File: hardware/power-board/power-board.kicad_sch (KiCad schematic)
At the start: 25 parts, among them J1 SW_SPST, J2 Main Board, J3 DMX512 Out Jack, J4 DMX512, K1 SPST-NO, K2 SPST-NO, P1 IEC320-C14, P2 IEC320-C13, P3 IEC320-C13, U1 NUD3112DMT1G, U2 MAX3075E

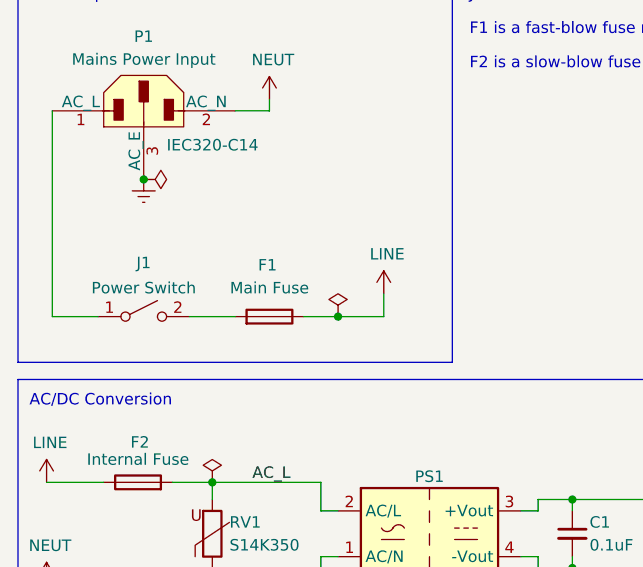
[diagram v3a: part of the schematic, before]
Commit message: Moved input fuse and changed power switch connector
The fuse is now before the power switch, which also makes routing a bit
easier.  Also switched the connector used for the power switch wires, to
something a bit less bulky.
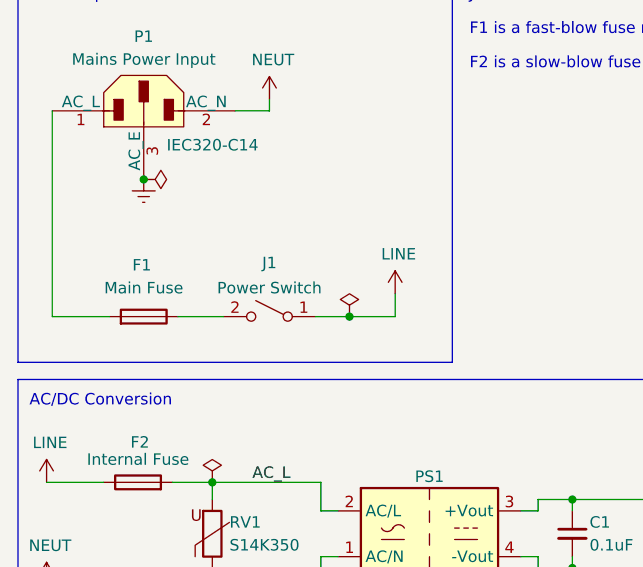
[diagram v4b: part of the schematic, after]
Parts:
- J1: footprint lib_fp:TE_MATE-N-LOK_350428-x_1x02_P6.35mm_Vertical -> Connector_Molex:Molex_Mega-Fit_76829-0002_2x01_P5.70mm_Vertical; Manufacturer TE Connectivity -> Molex; Manufacturer PN 350428-1 -> 0768290002; Supplier PN A1466-ND -> WM11975-ND
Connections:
- net LINE: now also J1.1 (A); no longer F1.1
- net at P1.1 (AC_L): now also F1.2; no longer J1.1 (A)
- net at J1.2 (B): now also F1.1; no longer F1.2
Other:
- moved on the sheet: F1, J1
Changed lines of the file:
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@@
   (junction (at 118.11 154.305) (diameter 0) (color 0 0 0 0)
   )
-  (junction (at 49.53 52.07) (diameter 0) (color 0 0 0 0)
+  (junction (at 50.8 52.07) (diameter 0) (color 0 0 0 0)
   )
   (junction (at 27.94 36.83) (diameter 0) (color 0 0 0 0)
@@
     (stroke (width 0) (type default))
   )
-  (wire (pts (xy 45.72 52.07) (xy 49.53 52.07))
+  (wire (pts (xy 46.99 52.07) (xy 50.8 52.07))
     (stroke (width 0) (type default))
   )
@@
     (stroke (width 0) (type default))
   )
-  (wire (pts (xy 33.02 52.07) (xy 38.1 52.07))
+  (wire (pts (xy 31.75 52.07) (xy 36.83 52.07))
     (stroke (width 0) (type default))
   )
@@
     (stroke (width 0) (type default))
   )
-  (wire (pts (xy 49.53 52.07) (xy 54.61 52.07))
+  (wire (pts (xy 50.8 52.07) (xy 55.88 52.07))
     (stroke (width 0) (type default))
   )
@@
     (stroke (width 0) (type default))
   )
-  (wire (pts (xy 54.61 52.07) (xy 54.61 49.53))
+  (wire (pts (xy 55.88 52.07) (xy 55.88 49.53))
     (stroke (width 0) (type default))
   )
@@
     (stroke (width 0) (type default))
   )
-  (wire (pts (xy 17.78 52.07) (xy 22.86 52.07))
+  (wire (pts (xy 17.78 52.07) (xy 24.13 52.07))
     (stroke (width 0) (type default))
   )
@@
     )
   )
-  (symbol (lib_id "Switch:SW_SPST") (at 27.94 52.07 0) (unit 1)
-    (in_bom yes) (on_board yes) (dnp no)
-    (property "Reference" "J1" (at 27.94 46.101 0)
-      (effects (font (size 1.27 1.27)))
-    )
-    (property "Value" "SW_SPST" (at 27.94 48.4124 0)
-      (effects (font (size 1.27 1.27)) hide)
-    )
-    (property "Footprint" "lib_fp:TE_MATE-N-LOK_350428-x_1x02_P6.35mm_Vertical" (at 27.94 52.07 0)
-      (effects (font (size 1.27 1.27)) hide)
-    )
-    (property "Datasheet" "https://www.te.com/commerce/DocumentDelivery/DDEController?Action=srchrtrv&DocNm=350428&DocType=Customer+Drawing&DocLang=English" (at 27.94 52.07 0)
-      (effects (font (size 1.27 1.27)) hide)
-    )
-    (property "User Label" "Power Switch" (at 27.94 48.895 0)
-      (effects (font (size 1.27 1.27)))
-    )
-    (property "Description" "CONN HEADER VERT 2POS 6.35MM" (at 27.94 52.07 0)
-      (effects (font (size 1.27 1.27)) hide)
-    )
-    (property "Manufacturer" "TE Connectivity" (at 27.94 52.07 0)
-      (effects (font (size 1.27 1.27)) hide)
-    )
-    (property "Manufacturer PN" "350428-1" (at 27.94 52.07 0)
-      (effects (font (size 1.27 1.27)) hide)
-    )
-    (property "Supplier" "Digi-Key" (at 27.94 52.07 0)
-      (effects (font (size 1.27 1.27)) hide)
-    )
-    (property "Supplier PN" "A1466-ND" (at 27.94 52.07 0)
+  (symbol (lib_id "Switch:SW_SPST") (at 41.91 52.07 0) (mirror y) (unit 1)
+    (in_bom yes) (on_board yes) (dnp no)
+    (property "Reference" "J1" (at 41.91 46.101 0)
+      (effects (font (size 1.27 1.27)))
+    )
+    (property "Value" "SW_SPST" (at 41.91 48.4124 0)
+      (effects (font (size 1.27 1.27)) hide)
+    )
+    (property "Footprint" "Connector_Molex:Molex_Mega-Fit_76829-0002_2x01_P5.70mm_Vertical" (at 41.91 52.07 0)
+      (effects (font (size 1.27 1.27)) hide)
+    )
+    (property "Datasheet" "https://www.molex.com/pdm_docs/as/AS-76823-100.pdf" (at 41.91 52.07 0)
+      (effects (font (size 1.27 1.27)) hide)
+    )
+    (property "User Label" "Power Switch" (at 41.91 48.895 0)
+      (effects (font (size 1.27 1.27)))
+    )
+    (property "Description" "CONN HEADER VERT 2POS 5.70MM" (at 41.91 52.07 0)
+      (effects (font (size 1.27 1.27)) hide)
+    )
+    (property "Manufacturer" "Molex" (at 41.91 52.07 0)
+      (effects (font (size 1.27 1.27)) hide)
+    )
+    (property "Manufacturer PN" "0768290002" (at 41.91 52.07 0)
+      (effects (font (size 1.27 1.27)) hide)
+    )
+    (property "Supplier" "Digi-Key" (at 41.91 52.07 0)
+      (effects (font (size 1.27 1.27)) hide)
+    )
+    (property "Supplier PN" "WM11975-ND" (at 41.91 52.07 0)
       (effects (font (size 1.27 1.27)) hide)
     )
@@
     )
   )
-  (symbol (lib_id "power:LINE") (at 54.61 49.53 0) (unit 1)
-    (in_bom yes) (on_board yes) (dnp no)
-    (property "Reference" "#PWR04" (at 54.61 53.34 0)
-      (effects (font (size 1.27 1.27)) hide)
-    )
-    (property "Value" "LINE" (at 54.991 45.1358 0)
-      (effects (font (size 1.27 1.27)))
-    )
-    (property "Footprint" "" (at 54.61 49.53 0)
-      (effects (font (size 1.27 1.27)) hide)
-    )
-    (property "Datasheet" "" (at 54.61 49.53 0)
+  (symbol (lib_id "power:LINE") (at 55.88 49.53 0) (unit 1)
+    (in_bom yes) (on_board yes) (dnp no)
+    (property "Reference" "#PWR04" (at 55.88 53.34 0)
+      (effects (font (size 1.27 1.27)) hide)
+    )
+    (property "Value" "LINE" (at 56.261 45.1358 0)
+      (effects (font (size 1.27 1.27)))
+    )
+    (property "Footprint" "" (at 55.88 49.53 0)
+      (effects (font (size 1.27 1.27)) hide)
+    )
+    (property "Datasheet" "" (at 55.88 49.53 0)
       (effects (font (size 1.27 1.27)) hide)
     )
@@
     )
   )
-  (symbol (lib_id "power:PWR_FLAG") (at 49.53 52.07 0) (unit 1)
-    (in_bom yes) (on_board yes) (dnp no)
-    (property "Reference" "#FLG01" (at 49.53 50.165 0)
-      (effects (font (size 1.27 1.27)) hide)
-    )
-    (property "Value" "PWR_FLAG" (at 49.53 48.26 0)
-      (effects (font (size 1.27 1.27)) hide)
-    )
-    (property "Footprint" "" (at 49.53 52.07 0)
-      (effects (font (size 1.27 1.27)) hide)
-    )
-    (property "Datasheet" "~" (at 49.53 52.07 0)
+  (symbol (lib_id "power:PWR_FLAG") (at 50.8 52.07 0) (unit 1)
+    (in_bom yes) (on_board yes) (dnp no)
+    (property "Reference" "#FLG01" (at 50.8 50.165 0)
+      (effects (font (size 1.27 1.27)) hide)
+    )
+    (property "Value" "PWR_FLAG" (at 50.8 48.26 0)
+      (effects (font (size 1.27 1.27)) hide)
+    )
+    (property "Footprint" "" (at 50.8 52.07 0)
+      (effects (font (size 1.27 1.27)) hide)
+    )
+    (property "Datasheet" "~" (at 50.8 52.07 0)
       (effects (font (size 1.27 1.27)) hide)
     )
@@
     )
   )
-  (symbol (lib_id "Device:Fuse") (at 41.91 52.07 270) (mirror x) (unit 1)
-    (in_bom yes) (on_board yes) (dnp no)
-    (property "Reference" "F1" (at 40.64 46.355 90)
-      (effects (font (size 1.27 1.27)) (justify left))
-    )
-    (property "Value" "Fuse" (at 36.83 49.53 90)
+  (symbol (lib_id "Device:Fuse") (at 27.94 52.07 270) (mirror x) (unit 1)
+    (in_bom yes) (on_board yes) (dnp no)
+    (property "Reference" "F1" (at 26.67 46.355 90)
+      (effects (font (size 1.27 1.27)) (justify left))
+    )
+    (property "Value" "Fuse" (at 22.86 49.53 90)
       (effects (font (size 1.27 1.27)) (justify left) hide)
     )
-    (property "Footprint" "Fuse:Fuseholder_Cylinder-5x20mm_Bulgin_FX0457_Horizontal_Closed" (at 41.91 53.848 90)
-      (effects (font (size 1.27 1.27)) hide)
-    )
-    (property "Datasheet" "https://www.bulgin.com/products/pub/media/bulgin/data/Fuseholders.pdf" (at 41.91 52.07 0)
-      (effects (font (size 1.27 1.27)) hide)
-    )
-    (property "User Label" "Main Fuse" (at 41.91 48.895 90)
-      (effects (font (size 1.27 1.27)))
-    )
-    (property "Description" "FUSE HLDR CARTRIDGE 250V 10A PCB" (at 41.91 52.07 0)
-      (effects (font (size 1.27 1.27)) hide)
-    )
-    (property "Manufacturer" "Bulgin" (at 41.91 52.07 0)
-      (effects (font (size 1.27 1.27)) hide)
-    )
-    (property "Manufacturer PN" "FX0457" (at 41.91 52.07 0)
-      (effects (font (size 1.27 1.27)) hide)
-    )
-    (property "Supplier" "Digi-Key" (at 41.91 52.07 0)
-      (effects (font (size 1.27 1.27)) hide)
-    )
-    (property "Supplier PN" "708-1898-ND" (at 41.91 52.07 0)
+    (property "Footprint" "Fuse:Fuseholder_Cylinder-5x20mm_Bulgin_FX0457_Horizontal_Closed" (at 27.94 53.848 90)
+      (effects (font (size 1.27 1.27)) hide)
+    )
+    (property "Datasheet" "https://www.bulgin.com/products/pub/media/bulgin/data/Fuseholders.pdf" (at 27.94 52.07 0)
+      (effects (font (size 1.27 1.27)) hide)
+    )
+    (property "User Label" "Main Fuse" (at 27.94 48.895 90)
+      (effects (font (size 1.27 1.27)))
+    )
+    (property "Description" "FUSE HLDR CARTRIDGE 250V 10A PCB" (at 27.94 52.07 0)
+      (effects (font (size 1.27 1.27)) hide)
+    )
+    (property "Manufacturer" "Bulgin" (at 27.94 52.07 0)
+      (effects (font (size 1.27 1.27)) hide)
+    )
+    (property "Manufacturer PN" "FX0457" (at 27.94 52.07 0)
+      (effects (font (size 1.27 1.27)) hide)
+    )
+    (property "Supplier" "Digi-Key" (at 27.94 52.07 0)
+      (effects (font (size 1.27 1.27)) hide)
+    )
+    (property "Supplier PN" "708-1898-ND" (at 27.94 52.07 0)
       (effects (font (size 1.27 1.27)) hide)
     )
@@
       (effects (font (size 1.27 1.27)) hide)
     )
+    (property "Sim.Name" "kicad_builtin_varistor" (at 35.56 76.2 0)
+      (effects (font (size 1.27 1.27)) hide)
+    )
+    (property "Sim.Device" "SUBCKT" (at 35.56 76.2 0)
+      (effects (font (size 1.27 1.27)) hide)
+    )
+    (property "Sim.Pins" "1=A 2=B" (at 35.56 76.2 0)
+      (effects (font (size 1.27 1.27)) hide)
+    )
+    (property "Sim.Params" "threshold=1k" (at 35.56 76.2 0)
+      (effects (font (size 1.27 1.27)) hide)
+    )
+    (property "Sim.Library" "${KICAD7_SYMBOL_DIR}/Simulation_SPICE.sp" (at 35.56 76.2 0)
+      (effects (font (size 1.27 1.27)) hide)
+    )

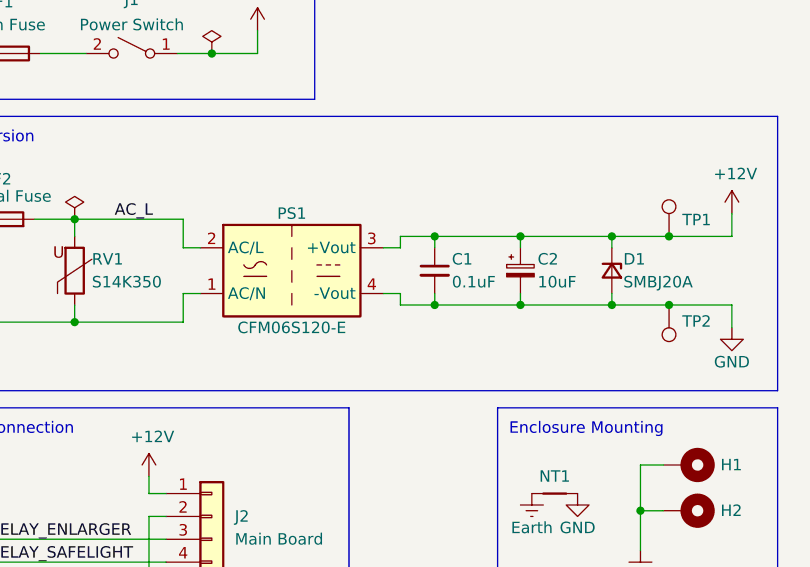
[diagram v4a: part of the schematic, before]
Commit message: Swap AC/DC converter for IRM-10-12 and update output capacitor
A bit more comfortable with this option versus the other one, since it
likely has more protection and filtering.  Still may want to rearrange
and reroute some of the output components, which are a bit cramped at
the moment.
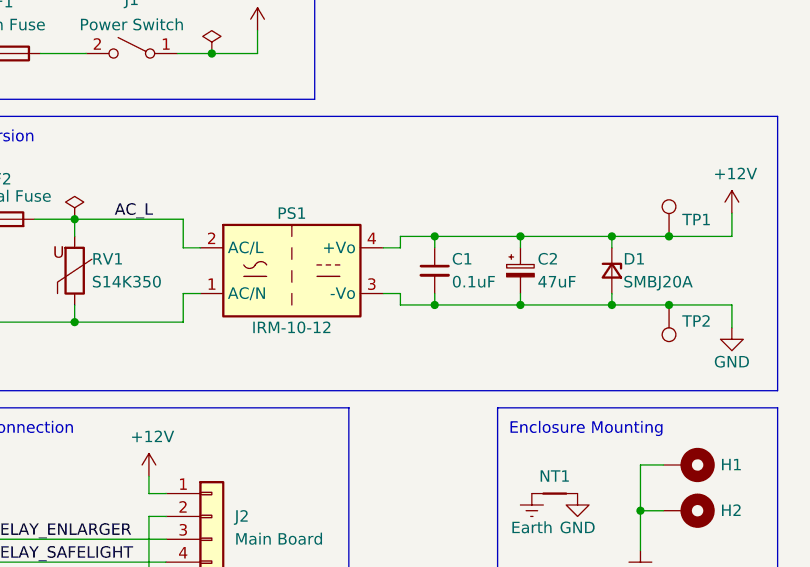
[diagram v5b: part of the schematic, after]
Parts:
- removed PS1: CFM06S120-E, lib_fp:Converter_ACDC_Cincom_CFM06Sxxx-E, symbol Project:CFM06S120-E
- added PS1: IRM-10-12, Converter_ACDC:Converter_ACDC_MeanWell_IRM-10-xx_THT, symbol Converter_ACDC:IRM-10-12
- C2: value 10uF -> 47uF; footprint Capacitor_SMD:CP_Elec_6.3x5.4 -> lib_fp:CP_Elec_8x10.2; Manufacturer PN EDK106M063A9GAA -> EDH476M063A9MAA; Supplier PN 399-6049-1-ND -> 399-18138-1-ND
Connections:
- net +12V: now also PS1.4 (+Vo)
- net AC_L: now also PS1.2 (AC/L)
- net GND: now also PS1.3 (-Vo)
- net NEUT: now also PS1.1 (AC/N)
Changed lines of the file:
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@@
-    )
-  )
-  (symbol (lib_id "Project:CFM06S120-E") (at 59.69 76.2 0) (unit 1)
-    (in_bom yes) (on_board yes) (dnp no)
-    (property "Reference" "PS1" (at 59.69 69.85 0)
-      (effects (font (size 1.27 1.27)))
-    )
-    (property "Value" "CFM06S120-E" (at 59.69 82.55 0)
-      (effects (font (size 1.27 1.27)))
-    )
-    (property "Footprint" "lib_fp:Converter_ACDC_Cincom_CFM06Sxxx-E" (at 59.69 85.09 0)
-      (effects (font (size 1.27 1.27)) hide)
-    )
-    (property "Datasheet" "https://www.cincon.com/productdownload/Datasheet-CFM06S-series.pdf" (at 59.69 86.995 0)
-      (effects (font (size 1.27 1.27)) hide)
-    )
-    (property "Description" "AC/DC CONVERTER 12V 6W" (at 59.69 76.2 0)
-      (effects (font (size 1.27 1.27)) hide)
-    )
-    (property "Manufacturer" "Cincon Electronics Co. LTD" (at 59.69 76.2 0)
-      (effects (font (size 1.27 1.27)) hide)
-    )
-    (property "Manufacturer PN" "CFM06S120-E" (at 59.69 76.2 0)
-      (effects (font (size 1.27 1.27)) hide)
-    )
-    (property "Supplier" "Digi-Key" (at 59.69 76.2 0)
-      (effects (font (size 1.27 1.27)) hide)
-    )
-    (property "Supplier PN" "2034-CFM06S120-E-ND" (at 59.69 76.2 0)
-      (effects (font (size 1.27 1.27)) hide)
-    )
-    (pin "1")
-    (pin "2")
-    (pin "3")
-    (pin "4")
-    (instances
-      (project "power-board"
-        (path "/31a301d9-d769-4a35-943a-fe3e3609e773"
-          (reference "PS1") (unit 1)
-        )
-      )
     )
   )
@@
       (effects (font (size 1.27 1.27)) (justify left))
     )
-    (property "Value" "10uF" (at 86.995 77.47 0)
-      (effects (font (size 1.27 1.27)) (justify left))
-    )
-    (property "Footprint" "Capacitor_SMD:CP_Elec_6.3x5.4" (at 85.09 76.2 0)
-      (effects (font (size 1.27 1.27)) hide)
-    )
-    (property "Datasheet" "https://content.kemet.com/datasheets/KEM_A4001_EDK.pdf" (at 85.09 76.2 0)
-      (effects (font (size 1.27 1.27)) hide)
-    )
-    (property "Description" "CAP ALUM 10UF 20% 63V SMD" (at 85.09 76.2 0)
+    (property "Value" "47uF" (at 86.995 77.47 0)
+      (effects (font (size 1.27 1.27)) (justify left))
+    )
+    (property "Footprint" "lib_fp:CP_Elec_8x10.2" (at 85.09 76.2 0)
+      (effects (font (size 1.27 1.27)) hide)
+    )
+    (property "Datasheet" "https://connect.kemet.com:7667/gateway/IntelliData-ComponentDocumentation/1.0/download/datasheet/EDH476M063A9MAA" (at 85.09 76.2 0)
+      (effects (font (size 1.27 1.27)) hide)
+    )
+    (property "Description" "CAP ALUM 47UF 20% 63V SMD" (at 85.09 76.2 0)
       (effects (font (size 1.27 1.27)) hide)
     )
@@
       (effects (font (size 1.27 1.27)) hide)
     )
-    (property "Manufacturer PN" "EDK106M063A9GAA" (at 85.09 76.2 0)
+    (property "Manufacturer PN" "EDH476M063A9MAA" (at 85.09 76.2 0)
       (effects (font (size 1.27 1.27)) hide)
     )
@@
       (effects (font (size 1.27 1.27)) hide)
     )
-    (property "Supplier PN" "399-6049-1-ND" (at 85.09 76.2 0)
+    (property "Supplier PN" "399-18138-1-ND" (at 85.09 76.2 0)
       (effects (font (size 1.27 1.27)) hide)
     )
@@
         )
       )
+    )
+  )
+  (symbol (lib_id "Converter_ACDC:IRM-10-12") (at 59.69 76.2 0) (unit 1)
+    (in_bom yes) (on_board yes) (dnp no)
+    (property "Reference" "PS1" (at 59.69 69.85 0)
+      (effects (font (size 1.27 1.27)))
+    )
+    (property "Value" "IRM-10-12" (at 59.69 82.55 0)
+      (effects (font (size 1.27 1.27)))
+    )
+    (property "Footprint" "Converter_ACDC:Converter_ACDC_MeanWell_IRM-10-xx_THT" (at 59.69 85.09 0)
+      (effects (font (size 1.27 1.27)) hide)
+    )
+    (property "Datasheet" "https://www.meanwell.com/Upload/PDF/IRM-10/IRM-10-SPEC.PDF" (at 59.69 86.36 0)
+      (effects (font (size 1.27 1.27)) hide)
+    )
+    (property "Description" "AC/DC CONVERTER 12V 10W" (at 59.69 76.2 0)
+      (effects (font (size 1.27 1.27)) hide)
+    )
+    (property "Manufacturer" "MEAN WELL" (at 59.69 76.2 0)
+      (effects (font (size 1.27 1.27)) hide)
+    )
+    (property "Manufacturer PN" "IRM-10-12" (at 59.69 76.2 0)
+      (effects (font (size 1.27 1.27)) hide)
+    )
+    (property "Supplier" "Mouser" (at 59.69 76.2 0)
+      (effects (font (size 1.27 1.27)) hide)
+    )
+    (property "Supplier PN" "709-IRM10-12" (at 59.69 76.2 0)
+      (effects (font (size 1.27 1.27)) hide)
+    )
+    (pin "1")
+    (pin "2")
+    (pin "3")
+    (pin "4")
+    (instances
+      (project "power-board"
+        (path "/31a301d9-d769-4a35-943a-fe3e3609e773"
+          (reference "PS1") (unit 1)
+        )
+      )
